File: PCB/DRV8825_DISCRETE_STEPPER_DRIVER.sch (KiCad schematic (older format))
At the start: 14 parts, among them U4 DRV8825PWPR

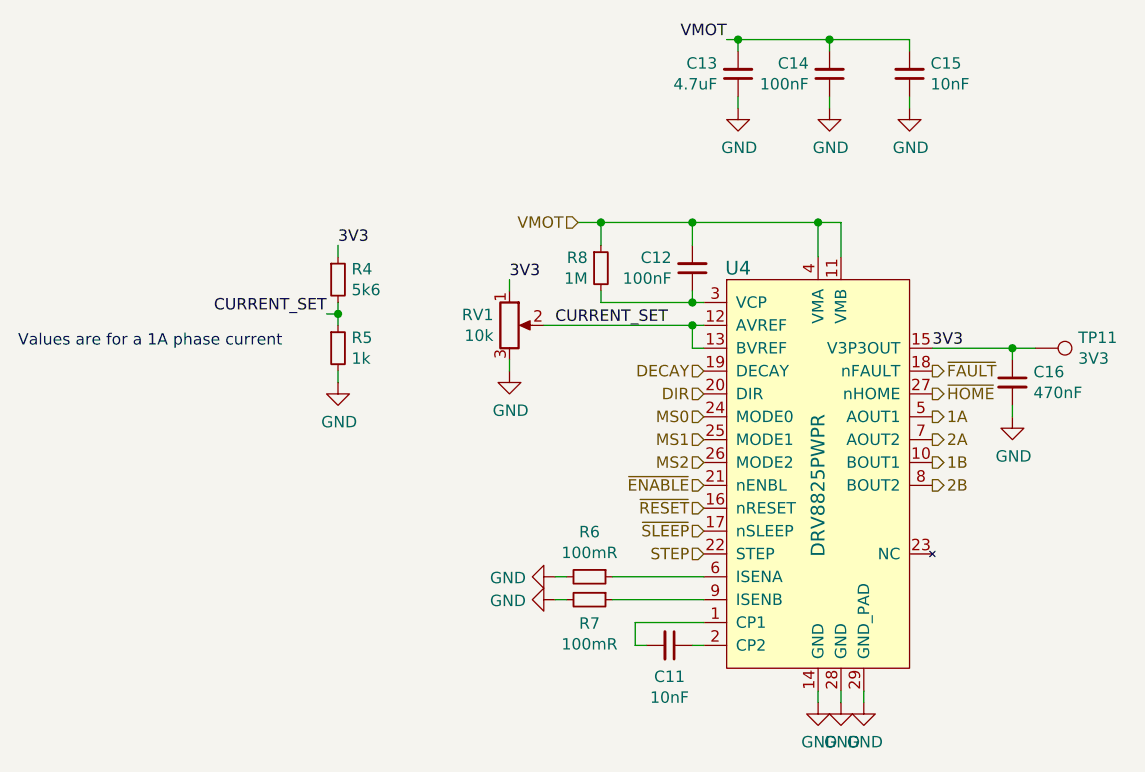
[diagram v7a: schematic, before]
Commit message: Replaced Tant Caps with Alu
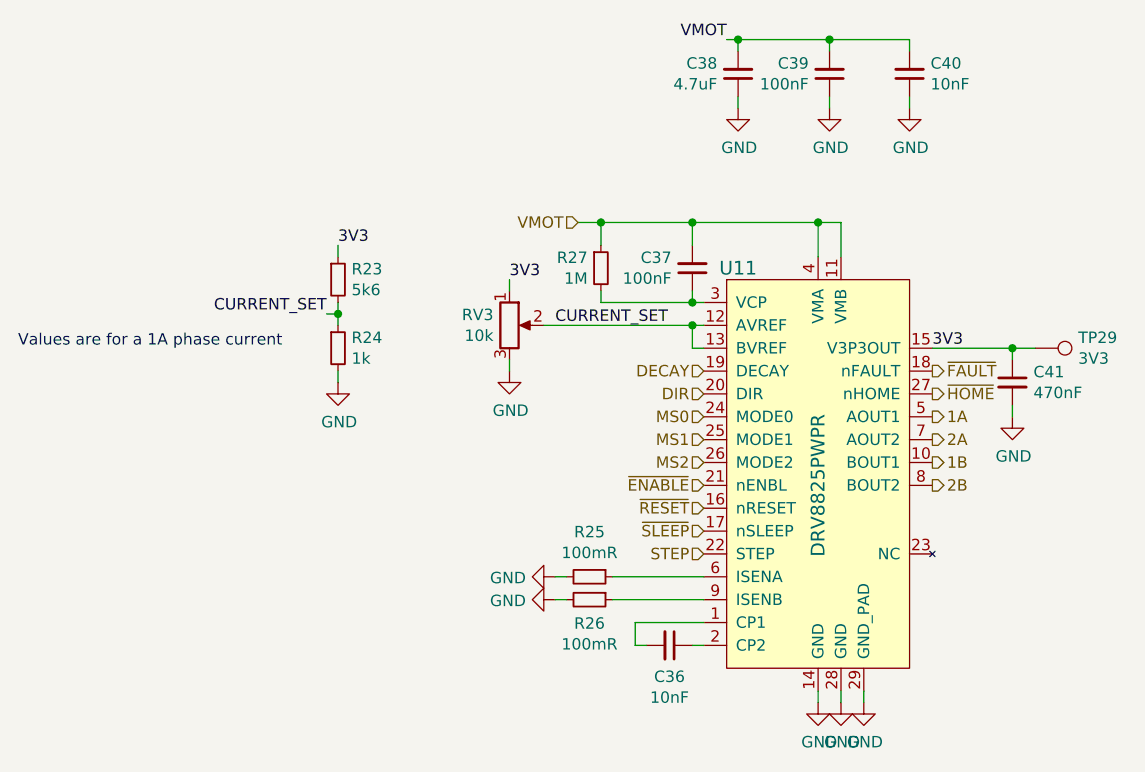
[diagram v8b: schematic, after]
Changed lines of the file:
@@
 $Descr A4 11693 8268
 encoding utf-8
-Sheet 4 22
+Sheet 15 22
 Title ""
 Date ""
@@
 AR Path="/5E8A6686/5E8D27A6/5E8D3351" Ref="U4"  Part="1"
 AR Path="/5E8813FF/5E8D27A6/5E8D3351" Ref="U11"  Part="1"
-F 0 "U4" H 5300 4500 60  0000 C CNN
+F 0 "U11" H 5300 4500 60  0000 C CNN
 F 1 "DRV8825PWPR" V 5650 3550 60  0000 C CNN
 F 2 "digikey-footprints:TSSOP-28-1EP_W4.40mm" H 5750 4050 60  0001 L CNN
@@
 AR Path="/5E8A6686/5E8D27A6/5E8D575F" Ref="C11"  Part="1"
 AR Path="/5E8813FF/5E8D27A6/5E8D575F" Ref="C36"  Part="1"
-F 0 "C11" V 5137 4850 50  0000 C CNN
+F 0 "C36" V 5137 4850 50  0000 C CNN
 F 1 "10nF" V 5228 4850 50  0000 C CNN
 F 2 "Capacitor_SMD:C_0603_1608Metric" H 5000 4850 50  0001 C CNN
@@
 AR Path="/5E8A6686/5E8D27A6/5E8D7A25" Ref="R6"  Part="1"
 AR Path="/5E8813FF/5E8D27A6/5E8D7A25" Ref="R25"  Part="1"
-F 0 "R6" V 4454 4550 50  0000 C CNN
+F 0 "R25" V 4454 4550 50  0000 C CNN
 F 1 "100mR" V 4545 4550 50  0000 C CNN
 F 2 "" H 4650 4550 50  0001 C CNN
@@
 AR Path="/5E8A6686/5E8D27A6/5E8D7F7E" Ref="R7"  Part="1"
 AR Path="/5E8813FF/5E8D27A6/5E8D7F7E" Ref="R26"  Part="1"
-F 0 "R7" V 4754 4650 50  0000 C CNN
+F 0 "R26" V 4754 4650 50  0000 C CNN
 F 1 "100mR" V 4845 4650 50  0000 C CNN
 F 2 "" H 4650 4650 50  0001 C CNN
@@
 AR Path="/5E8A6686/5E8D27A6/5E8DA337" Ref="C12"  Part="1"
 AR Path="/5E8813FF/5E8D27A6/5E8DA337" Ref="C37"  Part="1"
-F 0 "C12" H 5191 3154 50  0000 L CNN
+F 0 "C37" H 5191 3154 50  0000 L CNN
 F 1 "100nF" H 5191 3245 50  0000 L CNN
 F 2 "Capacitor_SMD:C_0603_1608Metric" H 5100 3200 50  0001 C CNN
@@
 AR Path="/5E8A6686/5E8D27A6/5E8DF1FC" Ref="RV1"  Part="1"
 AR Path="/5E8813FF/5E8D27A6/5E8DF1FC" Ref="RV3"  Part="1"
-F 0 "RV1" H 4230 3496 50  0000 R CNN
+F 0 "RV3" H 4230 3496 50  0000 R CNN
 F 1 "10k" H 4230 3405 50  0000 R CNN
 F 2 "Resistors:TRIMPOT-SMD-TC33X" H 4300 3450 50  0001 C CNN
@@
 AR Path="/5E8A6686/5E8D27A6/5E8E181B" Ref="C16"  Part="1"
 AR Path="/5E8813FF/5E8D27A6/5E8E181B" Ref="C41"  Part="1"
-F 0 "C16" H 6592 3746 50  0000 L CNN
+F 0 "C41" H 6592 3746 50  0000 L CNN
 F 1 "470nF" H 6592 3655 50  0000 L CNN
 F 2 "Capacitor_SMD:C_0603_1608Metric" H 6500 3700 50  0001 C CNN
@@
 AR Path="/5E8A6686/5E8D27A6/5E8E9760" Ref="C13"  Part="1"
 AR Path="/5E8813FF/5E8D27A6/5E8E9760" Ref="C38"  Part="1"
-F 0 "C13" H 5391 2304 50  0000 L CNN
+F 0 "C38" H 5391 2304 50  0000 L CNN
 F 1 "4.7uF" H 5391 2395 50  0000 L CNN
 F 2 "Capacitor_SMD:C_0603_1608Metric" H 5300 2350 50  0001 C CNN
@@
 AR Path="/5E8A6686/5E8D27A6/5E8E999E" Ref="C14"  Part="1"
 AR Path="/5E8813FF/5E8D27A6/5E8E999E" Ref="C39"  Part="1"
-F 0 "C14" H 5791 2304 50  0000 L CNN
+F 0 "C39" H 5791 2304 50  0000 L CNN
 F 1 "100nF" H 5791 2395 50  0000 L CNN
 F 2 "Capacitor_SMD:C_0603_1608Metric" H 5700 2350 50  0001 C CNN
@@
 AR Path="/5E8A6686/5E8D27A6/5E8E9DB5" Ref="C15"  Part="1"
 AR Path="/5E8813FF/5E8D27A6/5E8E9DB5" Ref="C40"  Part="1"
-F 0 "C15" H 5958 2304 50  0000 R CNN
+F 0 "C40" H 5958 2304 50  0000 R CNN
 F 1 "10nF" H 5958 2395 50  0000 R CNN
 F 2 "Capacitor_SMD:C_0603_1608Metric" H 6050 2350 50  0001 C CNN
@@
 AR Path="/5E8A6686/5E8D27A6/5E8B797B" Ref="R4"  Part="1"
 AR Path="/5E8813FF/5E8D27A6/5E8B797B" Ref="R23"  Part="1"
-F 0 "R4" H 3609 3296 50  0000 L CNN
+F 0 "R23" H 3609 3296 50  0000 L CNN
 F 1 "5k6" H 3609 3205 50  0000 L CNN
 F 2 "Resistor_SMD:R_0603_1608Metric" H 3550 3250 50  0001 C CNN
@@
 AR Path="/5E8A6686/5E8D27A6/5E8B7AF6" Ref="R5"  Part="1"
 AR Path="/5E8813FF/5E8D27A6/5E8B7AF6" Ref="R24"  Part="1"
-F 0 "R5" H 3609 3596 50  0000 L CNN
+F 0 "R24" H 3609 3596 50  0000 L CNN
 F 1 "1k" H 3609 3505 50  0000 L CNN
 F 2 "Resistor_SMD:R_0603_1608Metric" H 3550 3550 50  0001 C CNN
@@
 AR Path="/5E8A6686/5E8D27A6/5E8D6554" Ref="R8"  Part="1"
 AR Path="/5E8813FF/5E8D27A6/5E8D6554" Ref="R27"  Part="1"
-F 0 "R8" H 4642 3246 50  0000 R CNN
+F 0 "R27" H 4642 3246 50  0000 R CNN
 F 1 "1M" H 4642 3155 50  0000 R CNN
 F 2 "Resistor_SMD:R_0603_1608Metric" H 4700 3200 50  0001 C CNN
@@
 AR Path="/5E8A6686/5E8D27A6/5E958C53" Ref="TP11"  Part="1"
 AR Path="/5E8813FF/5E8D27A6/5E958C53" Ref="TP29"  Part="1"
-F 0 "TP11" V 6554 3738 50  0000 L CNN
+F 0 "TP29" V 6554 3738 50  0000 L CNN
 F 1 "3V3" V 6645 3738 50  0000 L CNN
 F 2 "custom:TestPoint_Pad_D1.5mm" H 6800 3550 50  0001 C CNN
